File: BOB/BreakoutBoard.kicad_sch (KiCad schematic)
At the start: 2 parts, among them J3 1706013

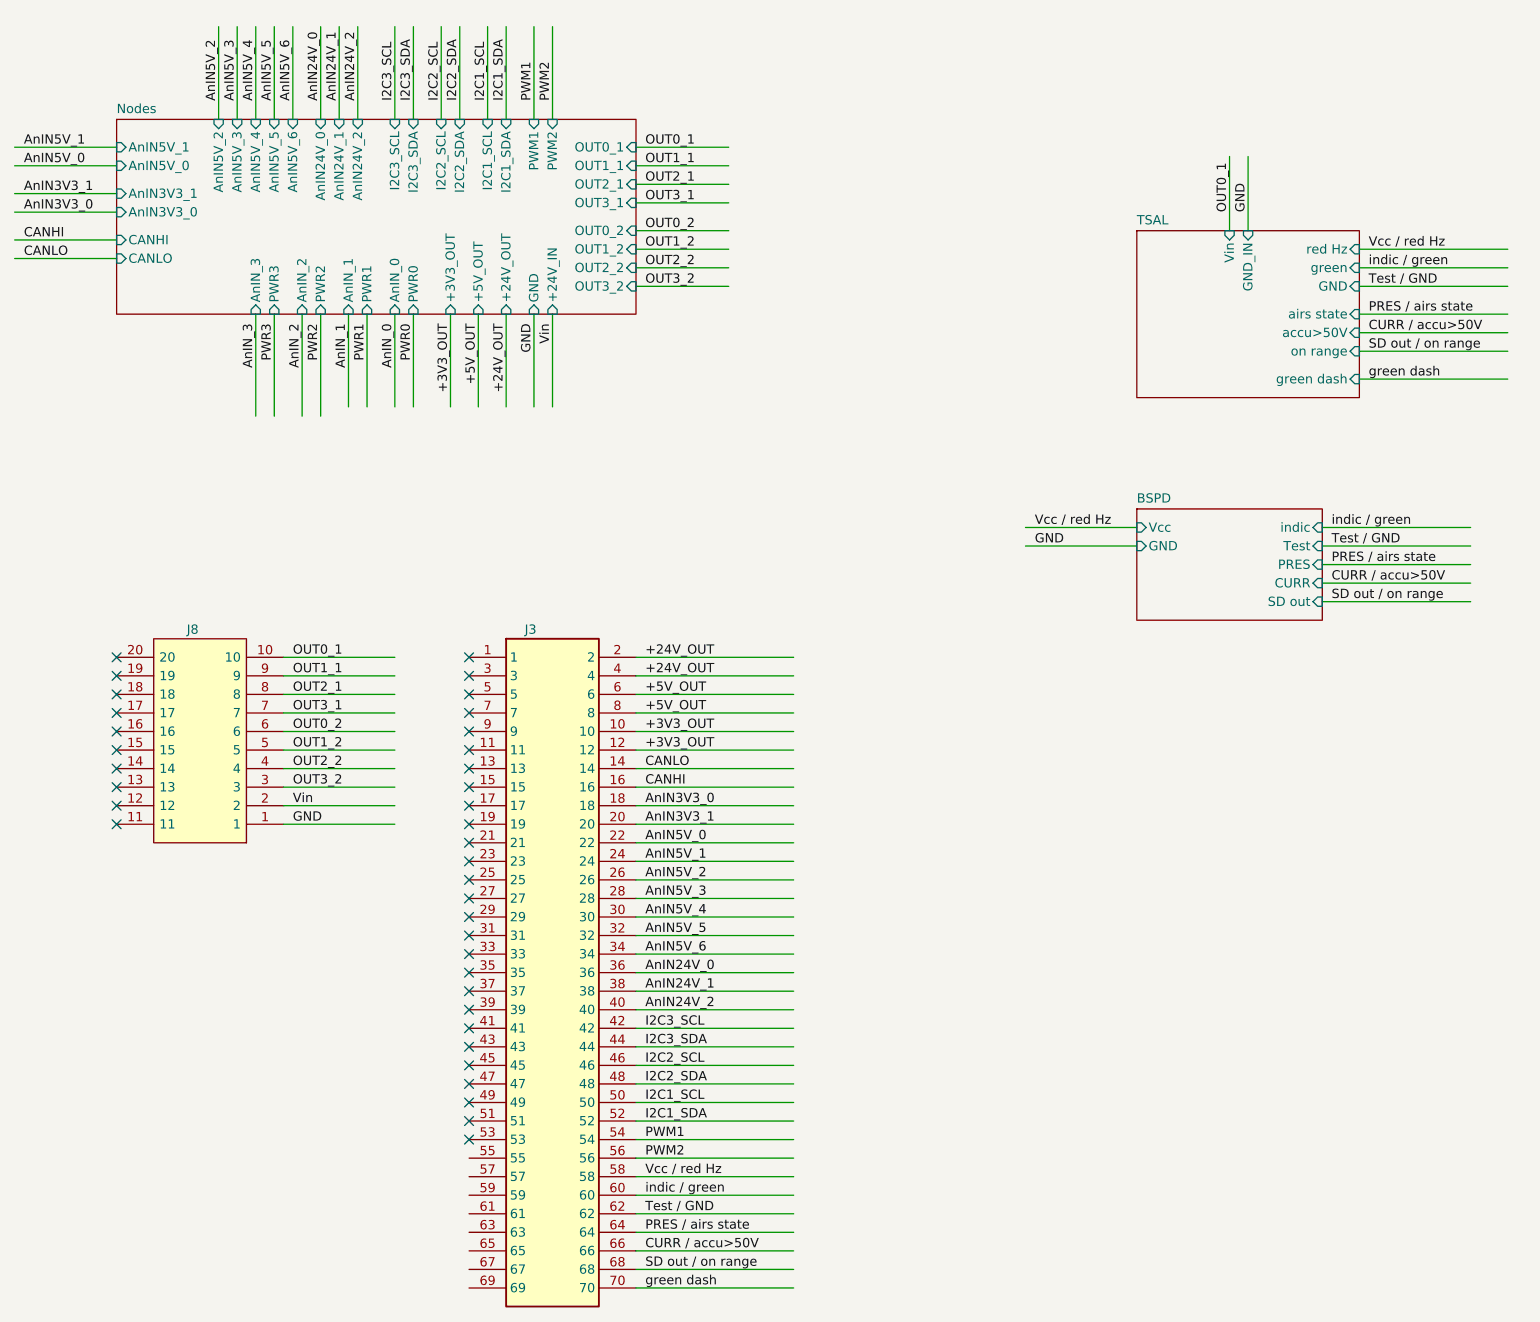
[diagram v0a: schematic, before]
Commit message: v2.2.1
-TSAL now connected to +24V_IN instead of OUT0_1
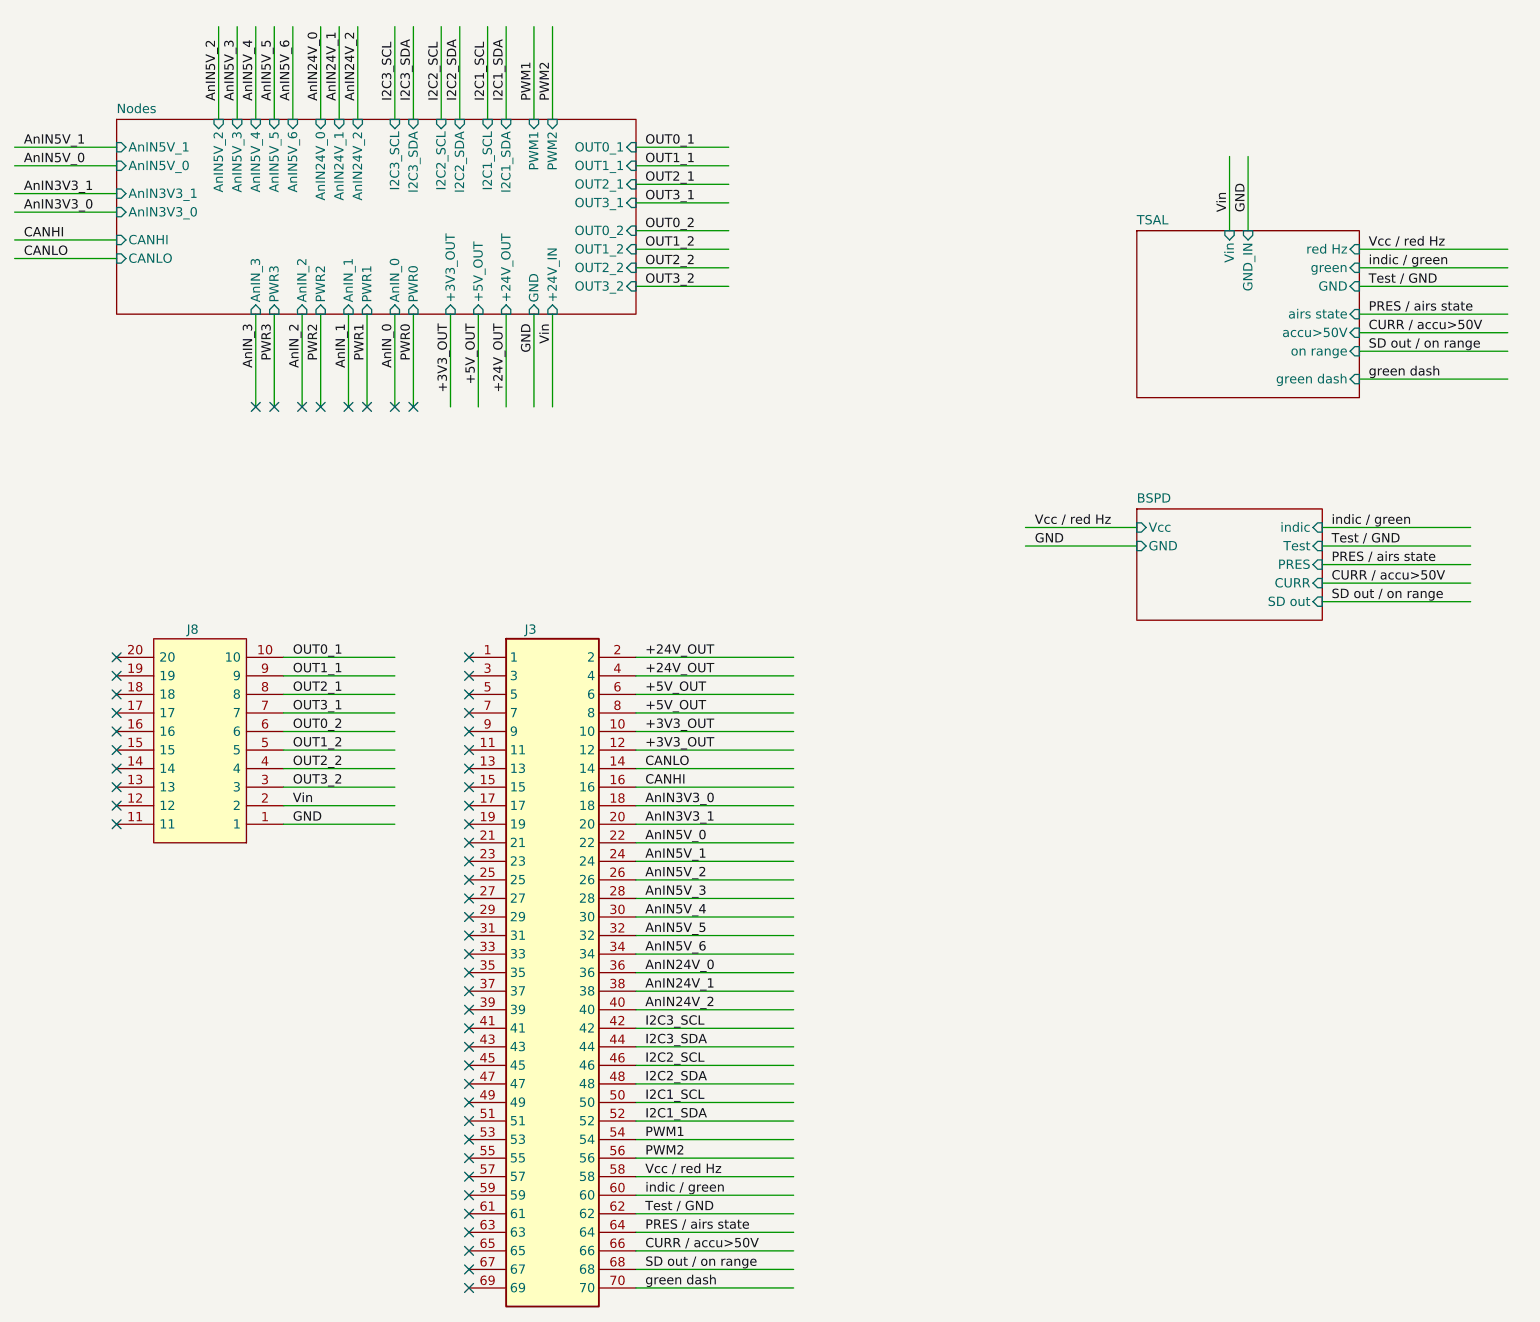
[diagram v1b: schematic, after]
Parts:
- J3: footprint Connector_Phoenix_SPT:1706013 -> Connector_Phoenix_SPT:35_con_Phoenix; symbol 1706013:1706013 -> Connector:35_con_Phoenix; Height 12.6 -> (none); Manufacturer_Name Phoenix Contact -> (none); Manufacturer_Part_Number 1706013 -> (none); Mouser Part Number 651-1706013 -> (none); Mouser Price/Stock https://www.mouser.com/Search/Refine.aspx?Keyword=651-17060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 -> (none)
- J8: symbol Connector:1868115 -> Connector:10_pin_7.62_Phoenix
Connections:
- no-connect marks 37 -> 53
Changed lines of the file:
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@@
+	)
+	(no_connect
+		(at 147.32 246.38)
 	)
 	(no_connect
@@
 	)
 	(no_connect
+		(at 147.32 259.08)
+	)
+	(no_connect
+		(at 127 138.43)
+	)
+	(no_connect
+		(at 120.65 138.43)
+	)
+	(no_connect
 		(at 147.32 238.76)
 	)
 	(no_connect
+		(at 147.32 254)
+	)
+	(no_connect
 		(at 99.06 193.04)
 	)
 	(no_connect
+		(at 147.32 251.46)
+	)
+	(no_connect
+		(at 147.32 243.84)
+	)
+	(no_connect
 		(at 147.32 228.6)
 	)
@@
 	)
 	(no_connect
+		(at 124.46 138.43)
+	)
+	(no_connect
 		(at 147.32 175.26)
 	)
@@
 	)
 	(no_connect
+		(at 137.16 138.43)
+	)
+	(no_connect
 		(at 99.06 172.72)
 	)
@@
 	)
 	(no_connect
+		(at 139.7 138.43)
+	)
+	(no_connect
 		(at 147.32 205.74)
 	)
 	(no_connect
+		(at 147.32 241.3)
+	)
+	(no_connect
 		(at 147.32 233.68)
 	)
@@
 	)
 	(no_connect
+		(at 147.32 248.92)
+	)
+	(no_connect
+		(at 118.11 138.43)
+	)
+	(no_connect
 		(at 147.32 200.66)
 	)
@@
 	)
 	(no_connect
+		(at 133.35 138.43)
+	)
+	(no_connect
 		(at 147.32 213.36)
 	)
@@
 	)
 	(no_connect
+		(at 130.81 138.43)
+	)
+	(no_connect
 		(at 147.32 193.04)
 	)
@@
 	)
 	(no_connect
+		(at 147.32 256.54)
+	)
+	(no_connect
 		(at 147.32 198.12)
 	)
@@
 	(wire
 		(pts
+			(xy 118.11 138.43) (xy 118.11 125.73)
+		)
+		(stroke
+			(width 0)
+			(type default)
+		)
+	)
+	(wire
+		(pts
 			(xy 170.18 114.3) (xy 182.88 114.3)
 		)
@@
 	(wire
 		(pts
-			(xy 118.11 125.73) (xy 118.11 139.7)
-		)
-		(stroke
-			(width 0)
-			(type default)
-		)
-	)
-	(wire
-		(pts
 			(xy 170.18 218.44) (xy 191.77 218.44)
 		)
@@
 	(wire
 		(pts
-			(xy 127 125.73) (xy 127 139.7)
+			(xy 127 125.73) (xy 127 138.43)
 		)
 		(stroke
@@
 	(wire
 		(pts
-			(xy 124.46 125.73) (xy 124.46 139.7)
+			(xy 124.46 125.73) (xy 124.46 138.43)
 		)
 		(stroke
@@
 	(wire
 		(pts
-			(xy 120.65 125.73) (xy 120.65 139.7)
+			(xy 120.65 125.73) (xy 120.65 138.43)
 		)
 		(stroke
@@
 		)
 	)
+	(label "Vin"
+		(at 251.46 111.76 90)
+		(fields_autoplaced yes)
+		(effects
+			(font
+				(size 1.27 1.27)
+			)
+			(justify left bottom)
+		)
+	)
 	(label "GND"
 		(at 156.21 127 270)
@@
 		)
 	)
-	(label "OUT0_1"
-		(at 251.46 111.76 90)
-		(fields_autoplaced yes)
-		(effects
-			(font
-				(size 1.27 1.27)
-			)
-			(justify left bottom)
-		)
-	)
 	(label "AnIN24V_1"
 		(at 171.45 218.44 0)
@@
 	)
 	(symbol
-		(lib_id "Connector:1868115")
+		(lib_id "Connector:10_pin_7.62_Phoenix")
 		(at 121.92 195.58 180)
 		(unit 1)
@@
 	)
 	(symbol
-		(lib_id "1706013:1706013")
+		(lib_id "Connector:35_con_Phoenix")
 		(at 147.32 172.72 0)
 		(unit 1)
@@
 			)
 		)
-		(property "Footprint" "Connector_Phoenix_SPT:1706013"
+		(property "Footprint" "Connector_Phoenix_SPT:35_con_Phoenix"
 			(at 166.37 267.64 0)
 			(effects
@@
 			)
 		)
-		(property "Description" "PCB terminal block, nominal current: 6 A 160 V number of potentials: 20 pitch: 2.54 mm"
+		(property "Description" ""
 			(at 147.828 163.322 0)
 			(effects
@@
 				(hide yes)
 			)
-		)
-		(property "Height" "12.6"
-			(at 166.37 567.64 0)
-			(effects
-				(font
-					(size 1.27 1.27)
-				)
-				(justify left top)
-				(hide yes)
-			)
-		)
-		(property "Manufacturer_Name" "Phoenix Contact"
-			(at 166.37 667.64 0)
-			(effects
-				(font
-					(size 1.27 1.27)
-				)
-				(justify left top)
-				(hide yes)
-			)
-		)
-		(property "Manufacturer_Part_Number" "1706013"
-			(at 166.37 767.64 0)
-			(effects
-				(font
-					(size 1.27 1.27)
-				)
-				(justify left top)
-				(hide yes)
-			)
-		)
-		(property "Mouser Part Number" "651-1706013"
-			(at 166.37 867.64 0)
-			(effects
-				(font
-					(size 1.27 1.27)
-				)
-				(justify left top)
-				(hide yes)
-			)
-		)
-		(property "Mouser Price/Stock" "https://www.mouser.com/Search/Refine.aspx?Keyword=651-1706013"
-			(at 166.37 967.64 0)
-			(effects
-				(font
-					(size 1.27 1.27)
-				)
-				(justify left top)
-				(hide yes)
-			)
-		)
-		(property "Arrow Part Number" ""
-			(at 166.37 1067.64 0)
-			(effects
-				(font
-					(size 1.27 1.27)
-				)
-				(justify left top)
-				(hide yes)
-			)
-		)
-		(property "Arrow Price/Stock" ""
-			(at 166.37 1167.64 0)
-			(effects
-				(font
-					(size 1.27 1.27)
-				)
-				(justify left top)
-				(hide yes)
-			)

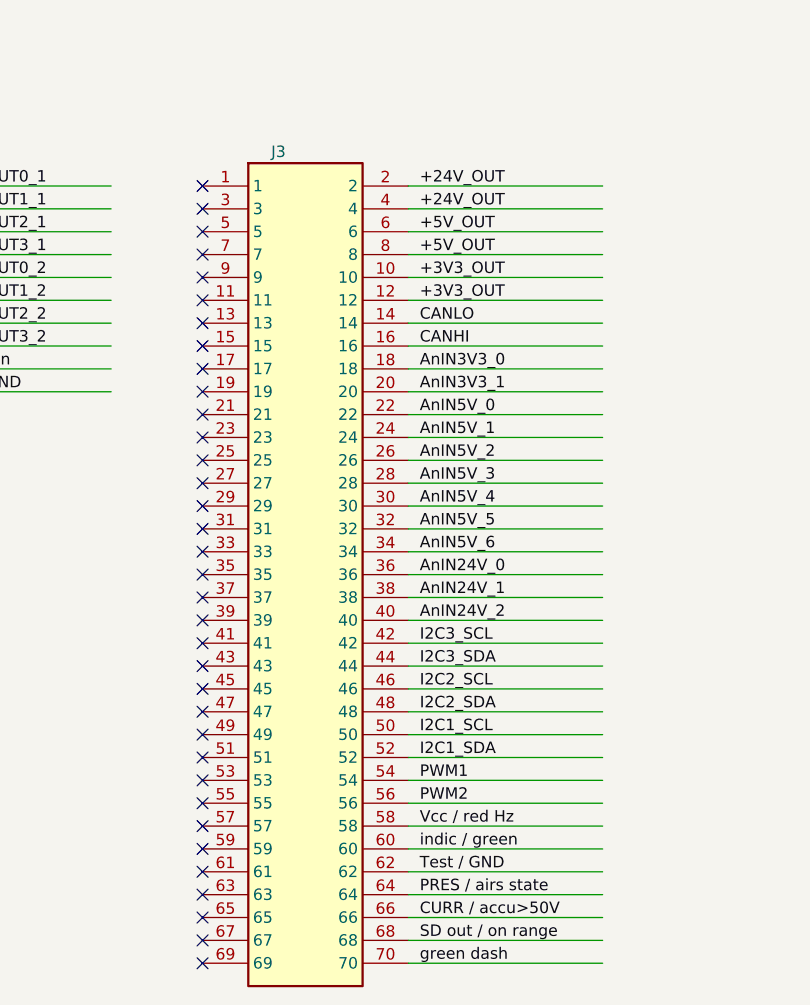
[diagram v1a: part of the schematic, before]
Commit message: v2.2.3
- New layout
- Removed from connectors:
* 2x +24V_OUT
* 1x +3V3_OUT
* 1x +5V_OUT
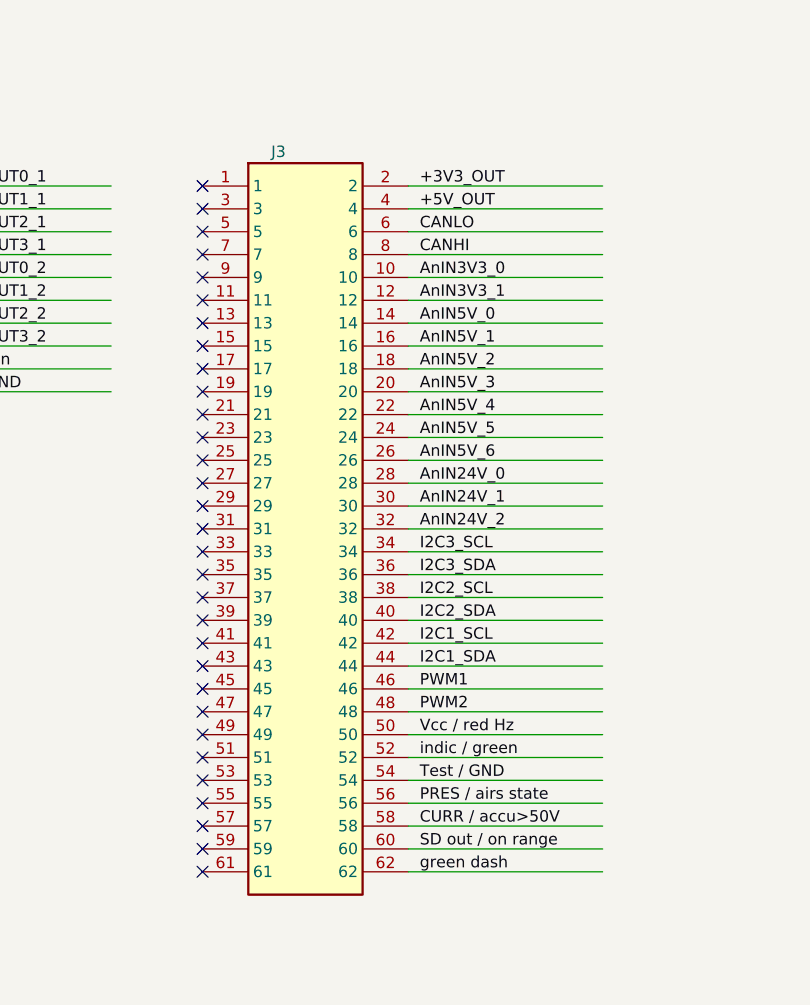
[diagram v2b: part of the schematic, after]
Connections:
- net +24V_OUT: no longer J3.2, J3.4
- net +3V3_OUT: now also J3.2; no longer J3.10, J3.12
- net +5V_OUT: now also J3.4; no longer J3.6, J3.8
- net AnIN24V_0: now also J3.28; no longer J3.36
- net AnIN24V_1: now also J3.30; no longer J3.38
- net AnIN24V_2: now also J3.32; no longer J3.40
- net AnIN3V3_0: now also J3.10; no longer J3.18
- net AnIN3V3_1: now also J3.12; no longer J3.20
- net AnIN5V_0: now also J3.14; no longer J3.22
- net AnIN5V_1: now also J3.16; no longer J3.24
- net AnIN5V_2: now also J3.18; no longer J3.26
- net AnIN5V_3: now also J3.20; no longer J3.28
- net AnIN5V_4: now also J3.22; no longer J3.30
- net AnIN5V_5: now also J3.24; no longer J3.32
- net AnIN5V_6: now also J3.26; no longer J3.34
- net CANHI: now also J3.8; no longer J3.16
- net CANLO: now also J3.6; no longer J3.14
- net CURR / accu>50V: now also J3.58; no longer J3.66
- net I2C1_SCL: now also J3.42; no longer J3.50
- net I2C1_SDA: now also J3.44; no longer J3.52
- net I2C2_SCL: now also J3.38; no longer J3.46
- net I2C2_SDA: now also J3.40; no longer J3.48
- net I2C3_SCL: now also J3.34; no longer J3.42
- net I2C3_SDA: now also J3.36; no longer J3.44
- net PRES / airs state: now also J3.56; no longer J3.64
- net PWM1: now also J3.46; no longer J3.54
- net PWM2: now also J3.48; no longer J3.56
- net SD out / on range: now also J3.60; no longer J3.68
- net Test / GND: now also J3.54; no longer J3.62
- net Vcc / red Hz: now also J3.50; no longer J3.58
- net green dash: now also J3.62; no longer J3.70
- net indic / green: now also J3.52; no longer J3.60
- no-connect marks 53 -> 49
